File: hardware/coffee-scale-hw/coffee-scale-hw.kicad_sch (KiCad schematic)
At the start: 72 parts, among them J1 PWR_IN, J2 OLED, J3 LOAD_CELL, Q1 AO3401A, Q2 AO3401A, Q3 PNP, SW1 SW_SPDT, SW2 SW_BACK, SW3 SW_L, SW4 SW_R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

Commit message: Working on HW design
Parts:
- gave numbers to parts that had none: 14
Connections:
- net GND: now also J1.1 (Pin_1); no longer J1.2 (Pin_2)
- net at SW1.2 (B): now also J1.2 (Pin_2); no longer J1.1 (Pin_1)
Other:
- moved on the sheet: J1
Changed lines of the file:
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@@
 	(wire
 		(pts
+			(xy 30.48 38.1) (xy 31.75 38.1)
+		)
+		(stroke
+			(width 0)
+			(type default)
+		)
+	)
+	(wire
+		(pts
 			(xy 85.09 35.56) (xy 85.09 36.83)
 		)
@@
 	(wire
 		(pts
+			(xy 30.48 35.56) (xy 33.02 35.56)
+		)
+		(stroke
+			(width 0)
+			(type default)
+		)
+	)
+	(wire
+		(pts
 			(xy 92.71 -60.96) (xy 92.71 -73.66)
 		)
@@
 	(wire
 		(pts
-			(xy 30.48 35.56) (xy 33.02 35.56)
-		)
-		(stroke
-			(width 0)
-			(type default)
-		)
-	)
-	(wire
-		(pts
 			(xy 254 121.92) (xy 260.35 121.92)
 		)
@@
 	(wire
 		(pts
-			(xy 30.48 38.1) (xy 31.75 38.1)
-		)
-		(stroke
-			(width 0)
-			(type default)
-		)
-	)
-	(wire
-		(pts
 			(xy 67.31 246.38) (xy 67.31 247.65)
 		)
@@
 		(dnp yes)
 		(fields_autoplaced yes)
-		(property "Reference" "U?"
+		(property "Reference" "U5"
 			(at 94.8533 -62.23 0)
 			(show_name no)
@@
 			(project "coffee-scale-hw"
 				(path "/9b9c2ebf-c052-4823-bb41-65b25094c161"
-					(reference "U?")
+					(reference "U5")
 					(unit 1)
 				)
@@
 		(in_pos_files no)
 		(dnp yes)
-		(property "Reference" "C?"
+		(property "Reference" "C22"
 			(at 46.99 -53.34 0)
 			(show_name no)
@@
 			(project "coffee-scale-hw"
 				(path "/9b9c2ebf-c052-4823-bb41-65b25094c161"
-					(reference "C?")
+					(reference "C22")
 					(unit 1)
 				)
@@
 		(in_pos_files no)
 		(dnp yes)
-		(property "Reference" "R?"
+		(property "Reference" "R24"
 			(at 106.68 -43.18 90)
 			(show_name no)
@@
 			(project "coffee-scale-hw"
 				(path "/9b9c2ebf-c052-4823-bb41-65b25094c161"
-					(reference "R?")
+					(reference "R24")
 					(unit 1)
 				)
@@
 		(in_pos_files no)
 		(dnp yes)
-		(property "Reference" "D?"
+		(property "Reference" "D2"
 			(at 77.5335 -45.72 0)
 			(show_name no)
@@
 			(project "coffee-scale-hw"
 				(path "/9b9c2ebf-c052-4823-bb41-65b25094c161"
-					(reference "D?")
+					(reference "D2")
 					(unit 1)
 				)
@@
 		(in_pos_files no)
 		(dnp yes)
-		(property "Reference" "C?"
+		(property "Reference" "C21"
 			(at 29.21 -101.6 0)
 			(show_name no)
@@
 			(project "coffee-scale-hw"
 				(path "/9b9c2ebf-c052-4823-bb41-65b25094c161"
-					(reference "C?")
+					(reference "C21")
 					(unit 1)
 				)
@@
 		(in_pos_files no)
 		(dnp yes)
-		(property "Reference" "R?"
+		(property "Reference" "R22"
 			(at 58.42 -95.25 90)
 			(show_name no)
@@
 			(project "coffee-scale-hw"
 				(path "/9b9c2ebf-c052-4823-bb41-65b25094c161"
-					(reference "R?")
+					(reference "R22")
 					(unit 1)
 				)
@@
 		(in_pos_files no)
 		(dnp yes)
-		(property "Reference" "C?"
+		(property "Reference" "C23"
 			(at 86.36 -71.12 0)
 			(show_name no)
@@
 			(project "coffee-scale-hw"
 				(path "/9b9c2ebf-c052-4823-bb41-65b25094c161"
-					(reference "C?")
+					(reference "C23")
 					(unit 1)
 				)
@@
 		(in_pos_files no)
 		(dnp yes)
-		(property "Reference" "C?"
+		(property "Reference" "C20"
 			(at 24.13 -88.9 0)
 			(show_name no)
@@
 			(project "coffee-scale-hw"
 				(path "/9b9c2ebf-c052-4823-bb41-65b25094c161"
-					(reference "C?")
+					(reference "C20")
 					(unit 1)
 				)
@@
 		(in_pos_files no)
 		(dnp yes)
-		(property "Reference" "R?"
+		(property "Reference" "R23"
 			(at 69.85 -45.72 90)
 			(show_name no)
@@
 			(project "coffee-scale-hw"
 				(path "/9b9c2ebf-c052-4823-bb41-65b25094c161"
-					(reference "R?")
+					(reference "R23")
 					(unit 1)
 				)
@@
 		(dnp yes)
 		(fields_autoplaced yes)
-		(property "Reference" "J?"
+		(property "Reference" "J5"
 			(at 25.4 -64.77 0)
 			(show_name no)
@@
 			(project "coffee-scale-hw"
 				(path "/9b9c2ebf-c052-4823-bb41-65b25094c161"
-					(reference "J?")
+					(reference "J5")
 					(unit 1)
 				)
@@
 	(symbol
 		(lib_id "Connector_Generic:Conn_01x02")
-		(at 25.4 35.56 0)
-		(mirror y)
+		(at 25.4 38.1 180)
 		(unit 1)
 		(body_style 1)
@@
 		(dnp no)
 		(property "Reference" "J1"
-			(at 22.86 35.56 0)
+			(at 22.86 38.1 0)
 			(show_name no)
 			(do_not_autoplace no)
@@
 		)
 		(property "Value" "PWR_IN"
-			(at 22.86 38.1 0)
+			(at 22.86 35.56 0)
 			(show_name no)
 			(do_not_autoplace no)
@@
 		)
 		(property "Footprint" "MyFootprints:Terminal_Pad_01x02-3x5mm"
-			(at 25.4 35.56 0)
+			(at 25.4 38.1 0)
 			(hide yes)
 			(show_name no)
@@
 		)
 		(property "Datasheet" ""
-			(at 25.4 35.56 0)
+			(at 25.4 38.1 0)
 			(hide yes)
 			(show_name no)
@@
 		)
 		(property "Description" "Generic connector, single row, 01x02, script generated (kicad-library-utils/schlib/autogen/connector/)"
-			(at 25.4 35.56 0)
+			(at 25.4 38.1 0)
 			(hide yes)
 			(show_name no)
@@
 		(dnp yes)
 		(fields_autoplaced yes)
-		(property "Reference" "U?"
+		(property "Reference" "U4"
 			(at 44.45 -109.22 0)
 			(show_name no)
@@
 			(project "coffee-scale-hw"
 				(path "/9b9c2ebf-c052-4823-bb41-65b25094c161"
-					(reference "U?")
+					(reference "U4")
 					(unit 1)
 				)
@@
 		(dnp yes)
 		(fields_autoplaced yes)
-		(property "Reference" "Q?"
+		(property "Reference" "Q4"
 			(at 49.53 -77.47 90)
 			(show_name no)
@@
 			(project "coffee-scale-hw"
 				(path "/9b9c2ebf-c052-4823-bb41-65b25094c161"
-					(reference "Q?")
+					(reference "Q4")
 					(unit 1)
 				)
@@
 		(in_pos_files no)
 		(dnp yes)
-		(property "Reference" "R?"
+		(property "Reference" "R21"
 			(at 26.67 -107.95 90)
 			(show_name no)
@@
 			(project "coffee-scale-hw"
 				(path "/9b9c2ebf-c052-4823-bb41-65b25094c161"
-					(reference "R?")
+					(reference "R21")
 					(unit 1)
 				)
@@
 		(in_pos_files no)
 		(dnp yes)
-		(property "Reference" "J?"
+		(property "Reference" "J4"
 			(at 15.24 -102.87 0)
 			(show_name no)
@@
 			(project "coffee-scale-hw"
 				(path "/9b9c2ebf-c052-4823-bb41-65b25094c161"
-					(reference "J?")
+					(reference "J4")
 					(unit 1)
 				)
@@
 		(dnp yes)
 		(fields_autoplaced yes)
-		(property "Reference" "Q?"
+		(property "Reference" "Q4"
 			(at 39.37 -77.47 90)
 			(show_name no)
@@
 			(project "coffee-scale-hw"
 				(path "/9b9c2ebf-c052-4823-bb41-65b25094c161"
-					(reference "Q?")
+					(reference "Q4")
 					(unit 2)
 				)

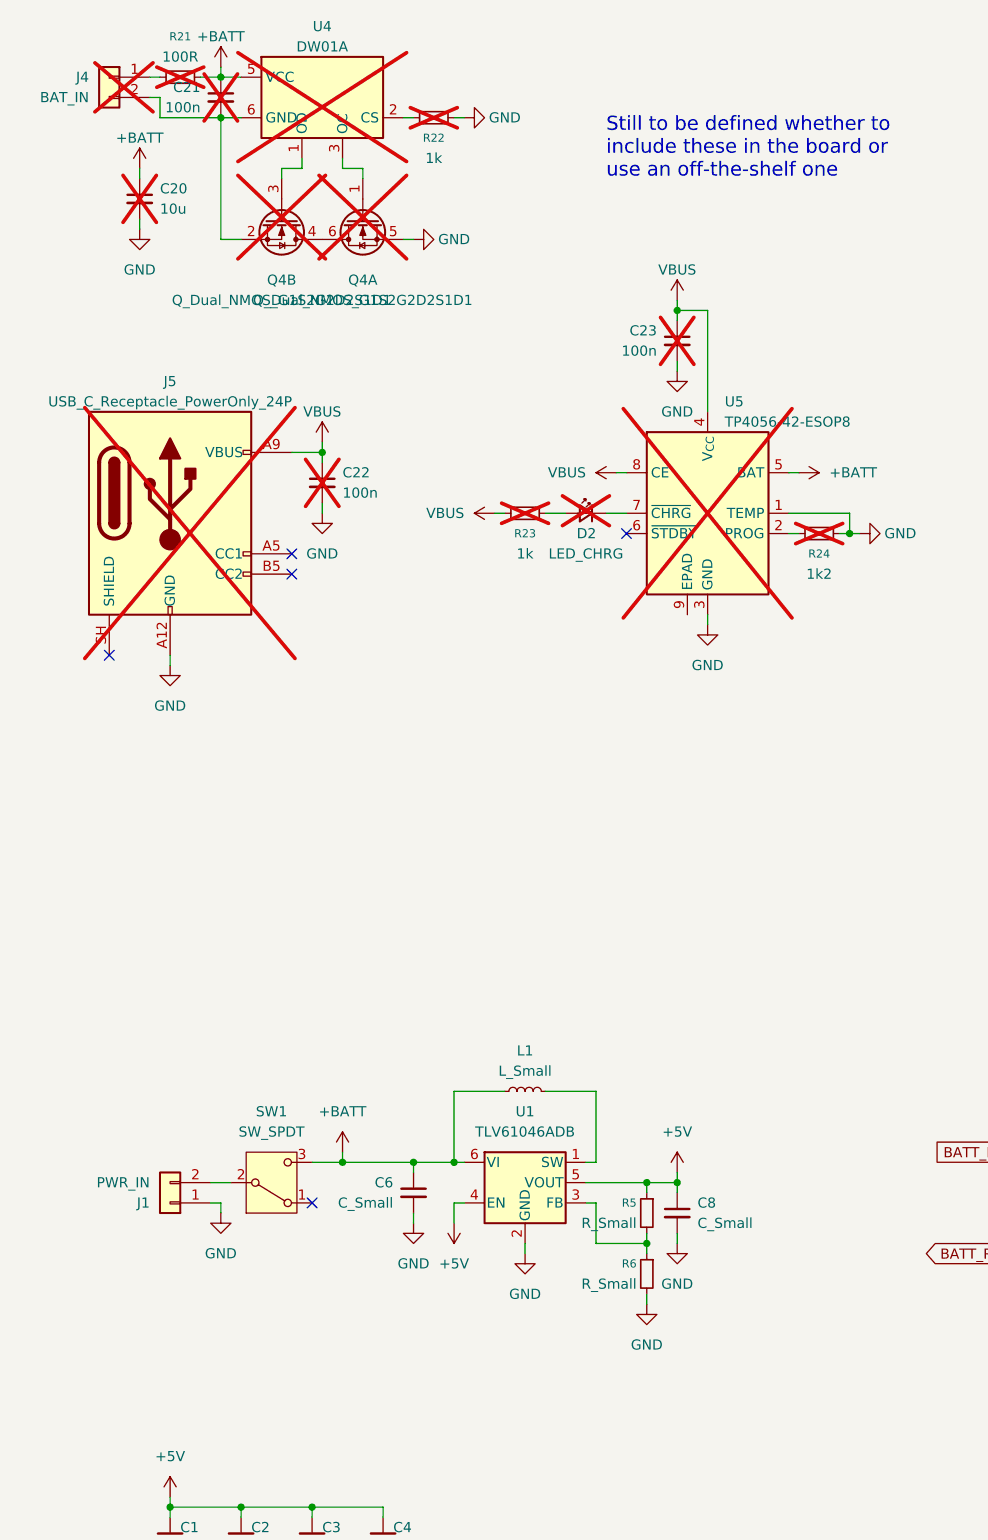
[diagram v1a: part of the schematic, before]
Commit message: Improved hx711 init
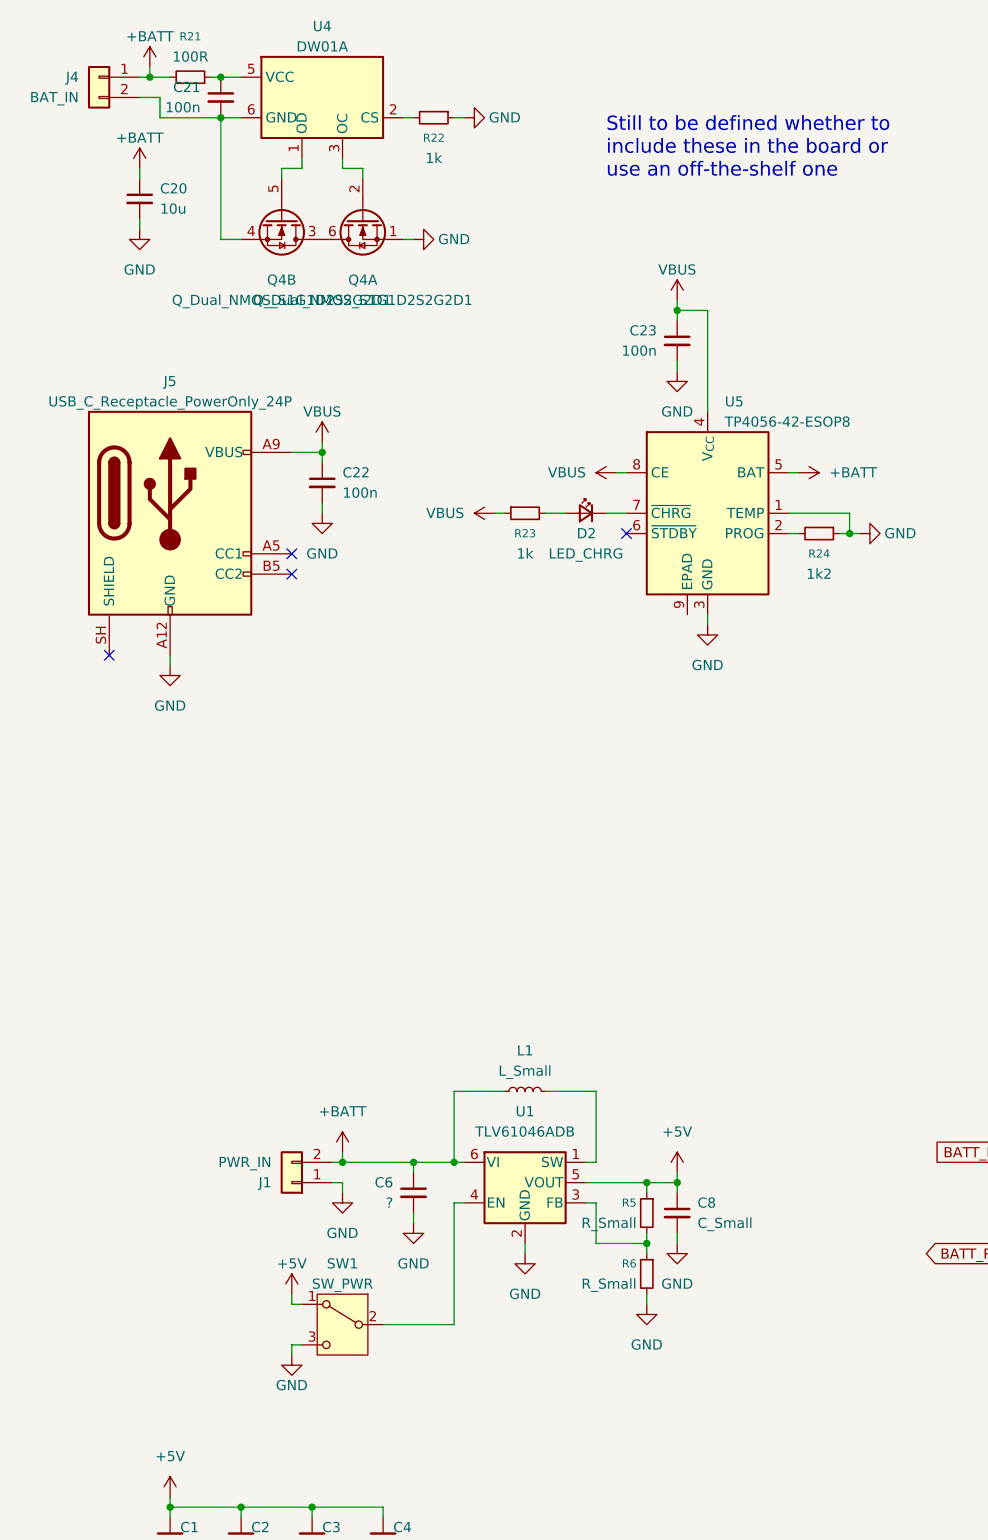
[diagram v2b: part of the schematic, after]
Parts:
- removed Q4: Q_Dual_NMOS_G1S2G2D2S1D1, symbol Transistor_FET:Q_Dual_NMOS_G1S2G2D2S1D1
- added Q4: Q_Dual_NMOS_S1G1D2S2G2D1, Package_TO_SOT_SMD:SOT-363_SC-70-6, symbol Transistor_FET:Q_Dual_NMOS_S1G1D2S2G2D1
- C20, C21, C22, C23, D2, J4, R21, R22, R23, R24, U4, U5: now fitted; now in the parts list
- C6: value C_Small -> ?
- J5: footprint (none) -> Connector_USB:USB_C_Receptacle_GCT_USB4125-xx-x_6P_TopMnt_Horizontal; now fitted; now in the parts list
- SW1: value SW_SPDT -> SW_PWR
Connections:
- net +5V: now also SW1.1 (A); no longer U1.4 (EN)
- net +BATT: now also J1.2 (Pin_2), J4.1 (Pin_1), R21.2; no longer C21.1, R21.1, SW1.3 (C), U4.5 (VCC)
- net GND: now also SW1.3 (C), Q4.1 (S)
- net at C21.2, J4.2 (Pin_2), U4.6 (GND): now also Q4.4 (S)
- net at SW1.2 (B): now also U1.4 (EN); no longer J1.2 (Pin_2)
- net at U4.1 (OD): now also Q4.5 (G)
- net at U4.3 (OC): now also Q4.2 (G)
- new net: Q4.3 (D), Q4.6 (D)
- new net: C21.1, R21.1, U4.5 (VCC)
- no-connect marks 8 -> 7
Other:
- moved on the sheet: J1, SW1

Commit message: Added LiPo battery USB-C charger
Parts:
- removed D1: LED_CHRG, LED_SMD:LED_0805_2012Metric, symbol Device:LED_Small
- removed J4: BAT_IN, MyFootprints:Terminal_Pad_01x02-3x5mm, symbol Connector_Generic:Conn_01x02
- removed Q2: AO3401A, Package_TO_SOT_SMD:SOT-23, symbol Transistor_FET:AO3401A
- removed R14: 10k, Resistor_SMD:R_0805_2012Metric, symbol Device:R_Small
- removed R15: 2k, Resistor_SMD:R_0805_2012Metric, symbol Device:R_Small
- J1: value PWR_IN -> BAT_IN
- renumbered D2 to D1
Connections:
- net +BATT: now also J1.1 (Pin_1); no longer J1.2 (Pin_2)
- net GND: no longer J1.1 (Pin_1)
- net at C21.2, Q4.4 (S), U4.6 (GND): now also J1.2 (Pin_2)
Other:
- note added: "Battery charge control"
- note added: "Battery protection against overcharge, overdischarge and/or overcurrent"
- note added: "Switching DC/DC converter to boost battery voltage (3.7V nominal) to fixed 5V"
- note removed: "Still to be defined whether to include these in the board or use an off-the-shelf one"
- moved on the sheet: C1, C10, C11, C12, C13, C14, C15, C16, C17, C18, C19, C2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
